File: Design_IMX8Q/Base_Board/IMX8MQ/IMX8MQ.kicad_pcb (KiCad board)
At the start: 8 copper layers, 50 x 80 mm, 95 parts, among them Q1 AO3401A, U1 MIMX8MQ6CVAHZAB, U2 IS43LQ32256A-062BLI, U4 MP8759GD-Z, U5 MP2263GD-Z, U6 SDINBDG4-8G, U7 MT25QUxxxxxx1xW7, X1 ABLNO, Y1 25MHz, Y2 27MHz

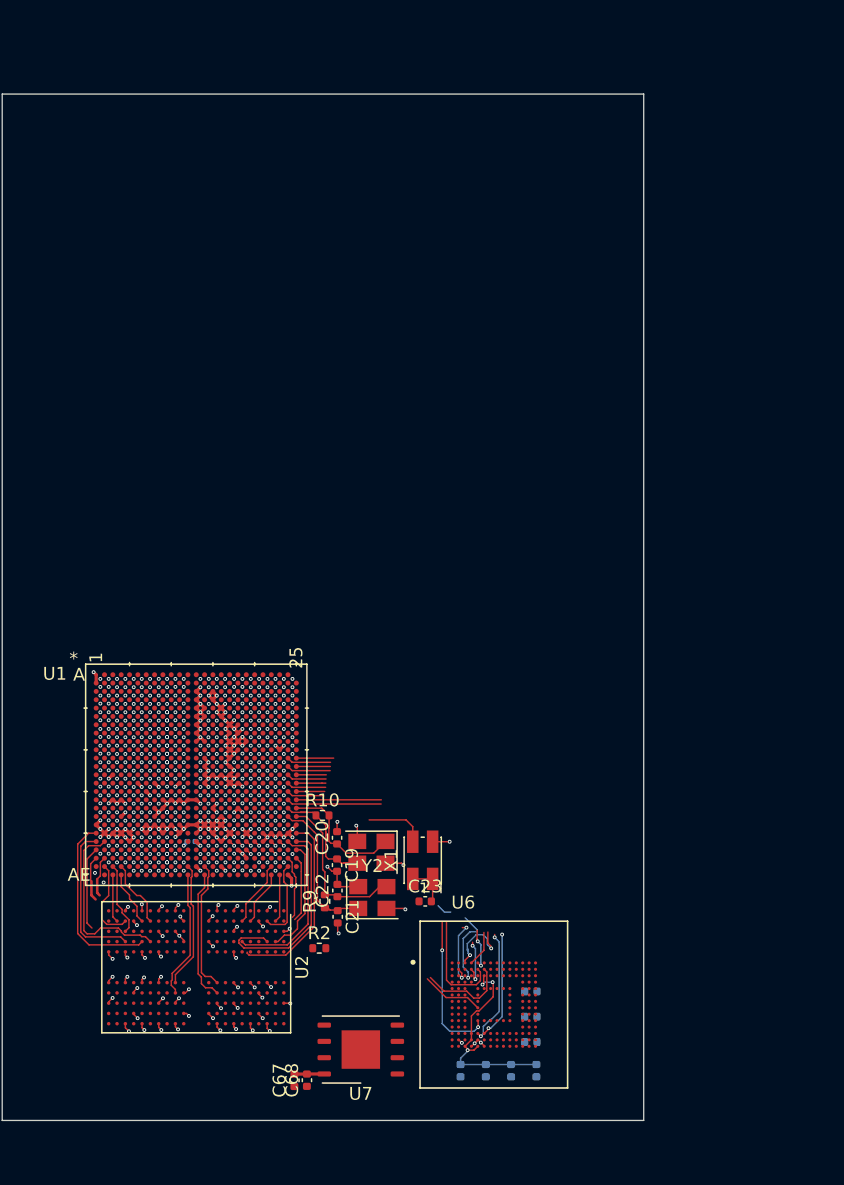
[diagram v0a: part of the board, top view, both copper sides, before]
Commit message: Adding color on LPDDR4 memory net
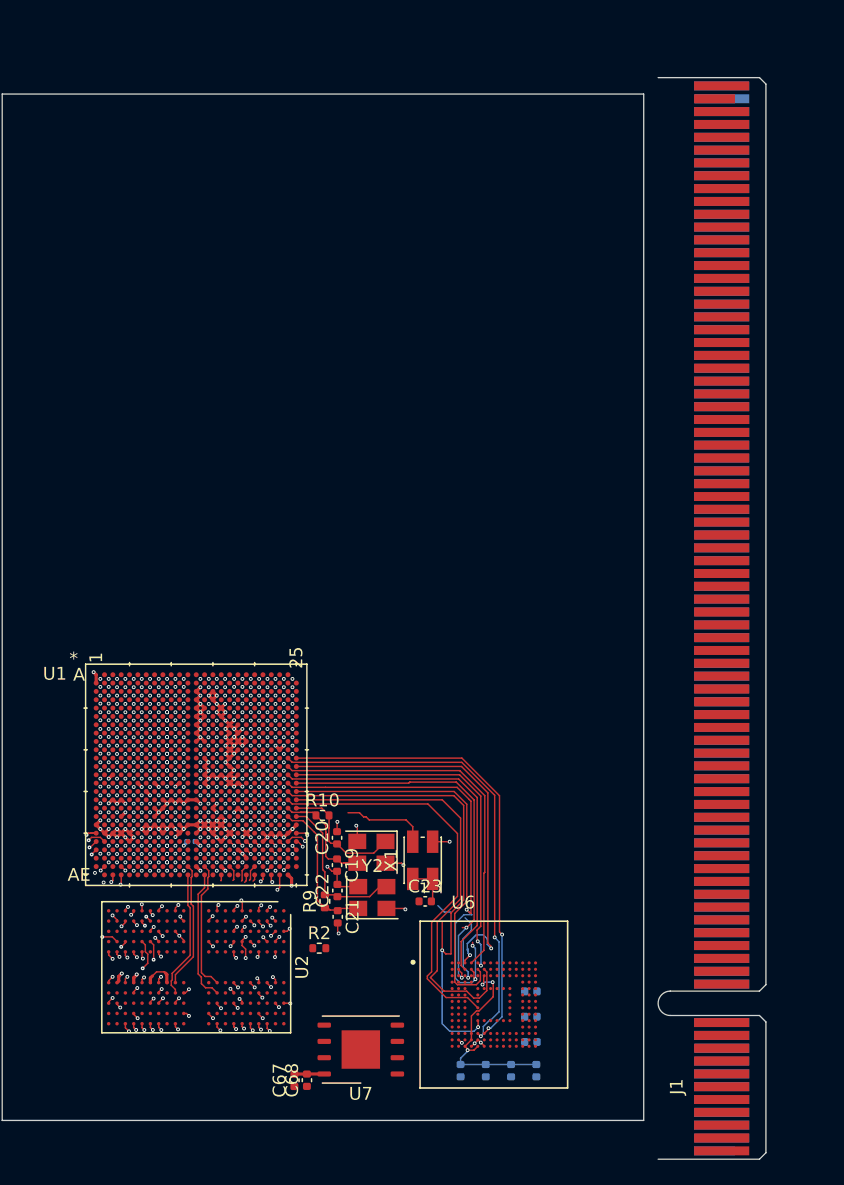
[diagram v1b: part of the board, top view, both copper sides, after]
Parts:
- added J1: Bus_PCI_Express_x16, Connector_PCBEdge:BUS_PCIexpress_x16, F.Cu at (114.0, 126.0)
- C24: value 0.1uF -> 4.7F
- C27: value 4.7F -> 0.1uF
- Y1: value 25MHz -> 27MHz
- Y2: value 27MHz -> 25MHz
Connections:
- U1 pad AB20: unconnected-(U1B-DRAM_DM1-PadAB20) -> DMI1_A
- U1 pad AB21: unconnected-(U1B-DRAM_DQS1_P-PadAB21) -> DQS1_A+
- U1 pad AB5: unconnected-(U1B-DRAM_DQS3_P-PadAB5) -> DQS1_B+
- U1 pad AB6: unconnected-(U1B-DRAM_DM3-PadAB6) -> DMI1_B
- U1 pad AC21: unconnected-(U1B-DRAM_DQS1_N-PadAC21) -> DQS1_A-
- U1 pad AC5: unconnected-(U1B-DRAM_DQS3_N-PadAC5) -> DQS1_B-
- U1 pad AC7: unconnected-(U1B-DRAM_AC28-PadAC7) -> CA2_B
- U1 pad AD17: unconnected-(U1B-DRAM_AC08-PadAD17) -> CA0_A
- U1 pad AD19: unconnected-(U1B-DRAM_AC12-PadAD19) -> CA4_A
- U1 pad AD20: unconnected-(U1B-DRAM_AC10-PadAD20) -> CA2_A
- U1 pad AD6: unconnected-(U1B-DRAM_AC31-PadAD6) -> CA5_B
- U1 pad AE16: unconnected-(U1B-DRAM_AC09-PadAE16) -> CA1_A
- U1 pad AE19: unconnected-(U1B-DRAM_AC13-PadAE19) -> CA5_A
- U1 pad AE20: unconnected-(U1B-DRAM_AC11-PadAE20) -> CA3_A
- U1 pad AE6: unconnected-(U1B-DRAM_AC30-PadAE6) -> CA4_B
- U1 pad AE7: unconnected-(U1B-DRAM_AC29-PadAE7) -> CA3_B
- U1 pad AE8: unconnected-(U1B-DRAM_AC32-PadAE8) -> CA0_B
- U1 pad AE9: unconnected-(U1B-DRAM_AC33-PadAE9) -> CA1_B
- U1 pad K10: unconnected-(U1H-VDD_GPU-PadK10) -> VDD_GPU
- U1 pad K12: unconnected-(U1H-VDD_SOC-PadK12) -> VDD_SOC
- U1 pad K13: unconnected-(U1K-VSSA_FPLL_ARM-PadK13) -> GND
- U1 pad K15: unconnected-(U1H-VDD_ARM-PadK15) -> VDD_ARM
- U1 pad K16: unconnected-(U1H-VDD_ARM-PadK16) -> VDD_ARM
- U1 pad L10: unconnected-(U1H-VDD_GPU-PadL10) -> VDD_GPU
- U1 pad L12: unconnected-(U1H-VDD_SOC-PadL12) -> VDD_SOC
- U1 pad L13: unconnected-(U1H-VDD_SOC-PadL13) -> VDD_SOC
- U1 pad L15: unconnected-(U1H-VDD_ARM-PadL15) -> VDD_ARM
- U1 pad L16: unconnected-(U1H-VDD_ARM-PadL16) -> VDD_ARM
- U1 pad M10: unconnected-(U1H-VDD_GPU-PadM10) -> VDD_GPU
- U1 pad M12: unconnected-(U1H-VDD_SOC-PadM12) -> VDD_SOC
- U1 pad M13: unconnected-(U1H-VDD_SOC-PadM13) -> VDD_SOC
- U1 pad M15: unconnected-(U1H-VDD_ARM-PadM15) -> VDD_ARM
- U1 pad M16: unconnected-(U1H-VDD_ARM-PadM16) -> VDD_ARM
- U1 pad N10: unconnected-(U1H-VDD_VPU-PadN10) -> VDD_VPU
- U1 pad N12: unconnected-(U1K-VSSA_SPLL_VIDEO2-PadN12) -> GND
- U1 pad N13: unconnected-(U1H-VDD_SOC-PadN13) -> VDD_SOC
- U1 pad P10: unconnected-(U1H-VDD_VPU-PadP10) -> VDD_VPU
- U1 pad P12: unconnected-(U1H-VDD_SOC-PadP12) -> VDD_SOC
- U1 pad P13: unconnected-(U1H-VDD_SOC-PadP13) -> VDD_SOC
- U1 pad P15: unconnected-(U1H-VDD_SOC-PadP15) -> VDD_SOC
- U1 pad P16: unconnected-(U1H-VDD_SOC-PadP16) -> VDD_SOC
- U1 pad R10: unconnected-(U1H-VDD_SOC-PadR10) -> VDD_SOC
- U1 pad R11: unconnected-(U1H-VDD_SOC-PadR11) -> VDD_SOC
- U1 pad R12: unconnected-(U1H-VDD_SOC-PadR12) -> VDD_SOC
- U1 pad R13: unconnected-(U1H-VDD_SOC-PadR13) -> VDD_SOC
- U1 pad R14: unconnected-(U1H-VDD_SOC-PadR14) -> VDD_SOC
- U1 pad R15: unconnected-(U1H-VDD_SOC-PadR15) -> VDD_SOC
- U1 pad R16: unconnected-(U1H-VDD_SOC-PadR16) -> VDD_SOC
- U1 pad T14: unconnected-(U1K-VSSA_SPLL_DRAM-PadT14) -> GND
- U1 pad T17: unconnected-(U1H-VDD_SOC-PadT17) -> VDD_SOC
- U1 pad U16: unconnected-(U1K-VSSA_FPLL-PadU16) -> GND
- U1 pad V17: unconnected-(U1K-VSSA_SPLL-PadV17) -> GND
- U1 pad V23: unconnected-(U1K-VSSA_XTAL_25M-PadV23) -> GND
- U1 pad W22: unconnected-(U1K-VSSA_XTAL_27M-PadW22) -> GND
- U2 pad AA11: unconnected-(U2B-DQ8_B-PadAA11) -> DRAM_DATA8_B
- U2 pad AA9: unconnected-(U2B-DQ15_B-PadAA9) -> DRAM_DATA15_B
- U2 pad B11: unconnected-(U2A-DQ8_A-PadB11) -> DRAM_DATA8_A
- U2 pad B9: unconnected-(U2A-DQ15_A-PadB9) -> DRAM_DATA15_A
- U2 pad C10: unconnected-(U2A-DMI1_A-PadC10) -> DMI1_A
- U2 pad C11: unconnected-(U2A-DQ9_A-PadC11) -> DRAM_DATA9_A
- U2 pad C9: unconnected-(U2A-DQ14_A-PadC9) -> DRAM_DATA14_A
- U2 pad D10: unconnected-(U2A-DQS1_T_A-PadD10) -> DQS1_A+
- U2 pad E10: unconnected-(U2A-DQS1_C_A-PadE10) -> DQS1_A-
- U2 pad E11: unconnected-(U2A-DQ10_A-PadE11) -> DRAM_DATA10_A
- U2 pad E9: unconnected-(U2A-DQ13_A-PadE9) -> DRAM_DATA13_A
- U2 pad F11: unconnected-(U2A-DQ11_A-PadF11) -> DRAM_DATA11_A
- U2 pad F9: unconnected-(U2A-DQ12_A-PadF9) -> DRAM_DATA12_A
- U2 pad H10: unconnected-(U2A-CA3_A-PadH10) -> CA3_A
- U2 pad H11: unconnected-(U2A-CA4_A-PadH11) -> CA4_A
- U2 pad H2: unconnected-(U2A-CA0_A-PadH2) -> CA0_A
- U2 pad H9: unconnected-(U2A-CA2_A-PadH9) -> CA2_A
- U2 pad J11: unconnected-(U2A-CA5_A-PadJ11) -> CA5_A
- U2 pad J2: unconnected-(U2A-CA1_A-PadJ2) -> CA1_A
- U2 pad P11: unconnected-(U2B-CA5_B-PadP11) -> CA5_B
- U2 pad P2: unconnected-(U2B-CA1_B-PadP2) -> CA1_B
- U2 pad R10: unconnected-(U2B-CA3_B-PadR10) -> CA3_B
- U2 pad R11: unconnected-(U2B-CA4_B-PadR11) -> CA4_B
- U2 pad R2: unconnected-(U2B-CA0_B-PadR2) -> CA0_B
- U2 pad R9: unconnected-(U2B-CA2_B-PadR9) -> CA2_B
- U2 pad U11: unconnected-(U2B-DQ11_B-PadU11) -> DRAM_DATA11_B
- U2 pad U9: unconnected-(U2B-DQ12_B-PadU9) -> DRAM_DATA12_B
- U2 pad V10: unconnected-(U2B-DQS1_C_B-PadV10) -> DQS1_B-
- U2 pad V11: unconnected-(U2B-DQ10_B-PadV11) -> DRAM_DATA10_B
- U2 pad V9: unconnected-(U2B-DQ13_B-PadV9) -> DRAM_DATA13_B
- U2 pad W10: unconnected-(U2B-DQS1_T_B-PadW10) -> DQS1_B+
- U2 pad Y10: unconnected-(U2B-DMI1_B-PadY10) -> DMI1_B
- U2 pad Y11: unconnected-(U2B-DQ9_B-PadY11) -> DRAM_DATA9_B
- U2 pad Y9: unconnected-(U2B-DQ14_B-PadY9) -> DRAM_DATA14_B
- Y1 pad 1: Net-(U1F-XTALI_25M) -> Net-(U1F-XTALO_27M)
- Y1 pad 3: Net-(U1F-XTALO_25M) -> Net-(U1F-XTALI_27M)
- Y2 pad 1: Net-(U1F-XTALO_27M) -> Net-(U1F-XTALI_25M)
- Y2 pad 3: Net-(U1F-XTALI_27M) -> Net-(U1F-XTALO_25M)
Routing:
- net SD1_DATA5: track 6.90 -> 36.1 mm, vias 2 -> 3
- net SD1_DATA4: track 10.3 -> 36.0 mm
- net SD1_CLK: track 11.3 -> 36.3 mm
- net SD1_CMD: track 12.5 -> 37.2 mm
- net SD1_nRST: track 14.5 -> 38.5 mm
- net SD1_DATA0: track 8.78 -> 32.8 mm
- net SD1_DATA1: track 6.20 -> 29.8 mm
- net VDD_1v8: track 0.00 -> 23.3 mm, vias 0 -> 27
- net SD1_DATA2: track 5.56 -> 28.9 mm
- net SD1_DATA3: track 7.61 -> 30.0 mm
- net SD1_DATA6: track 10.7 -> 31.1 mm
- net SD1_DATA7: track 13.7 -> 33.8 mm
- net SD1_STROBE: track 12.3 -> 31.5 mm
- net DMI0_B: track 5.69 -> 0.00 mm
- net DRAM_DATA6_A: track 16.7 -> 11.4 mm, vias 0 -> 2
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- added copper zone on In2.Cu, net VDD_1v8

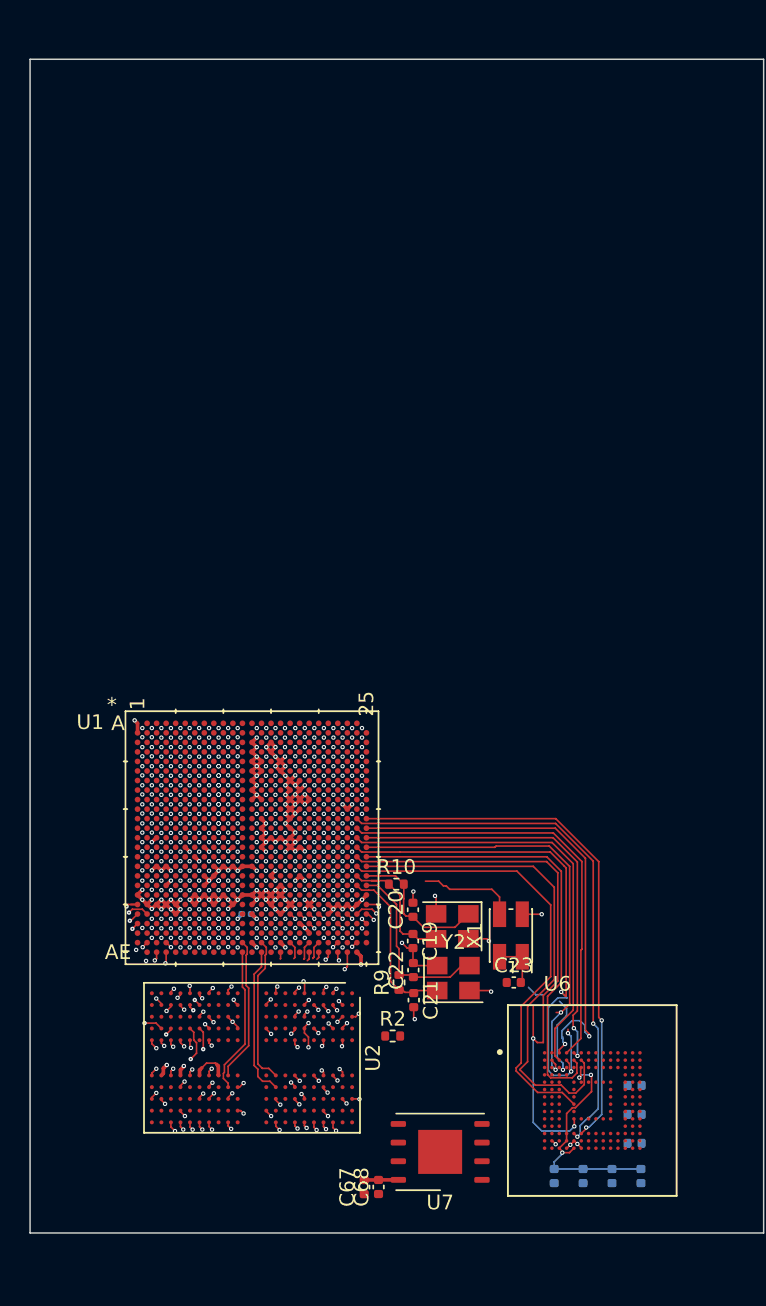
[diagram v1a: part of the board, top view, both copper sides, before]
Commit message: Add library to WIFI/BLE
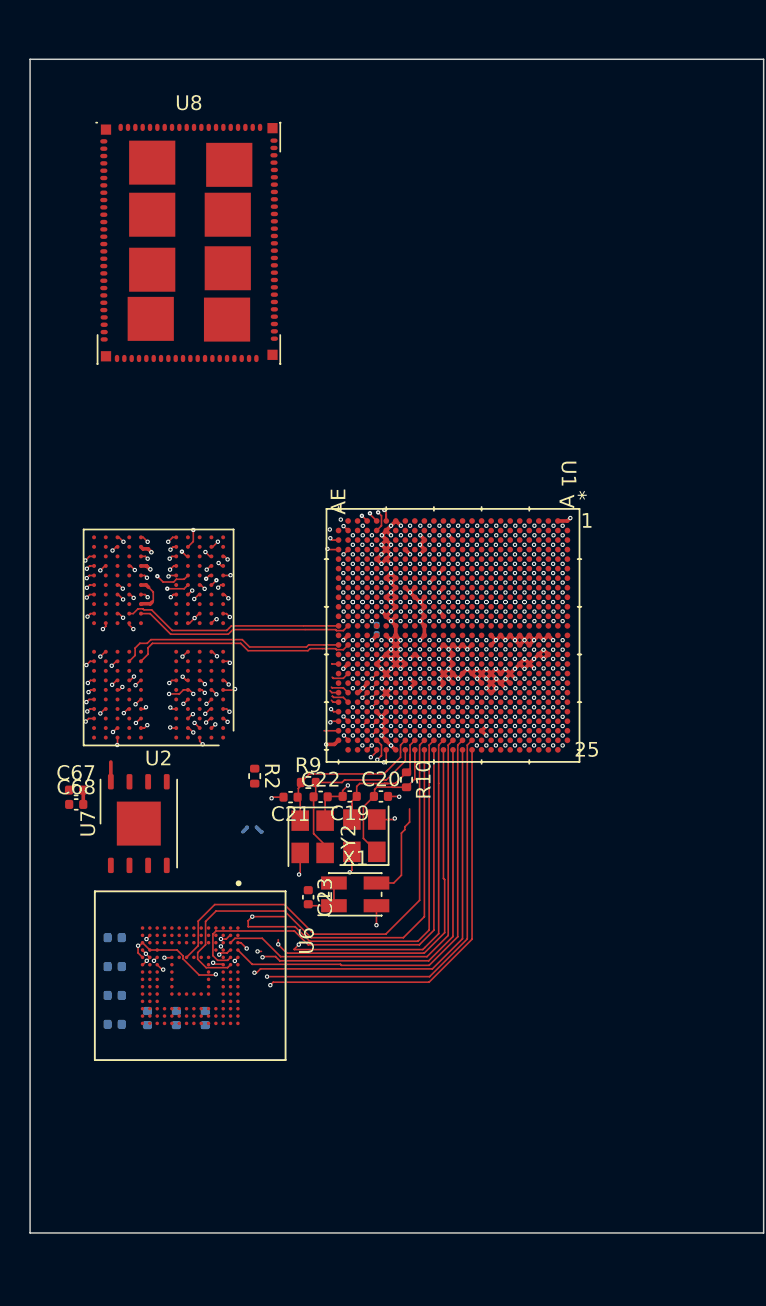
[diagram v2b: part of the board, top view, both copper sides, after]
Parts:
- added U8: ~, _W_SBC:WG3221-00_DTS_R01, F.Cu at (68.7, 56.2)
- moved C24 37.3 mm to (63.7, 109.4), turned to 0 degrees
- moved C25 36.1 mm to (63.7, 107.4), turned to 0 degrees
- moved C26 35.0 mm to (63.7, 105.5), turned to 0 degrees
- moved C28 34.3 mm to (65.9, 109.0), turned to -90 degrees
- moved C27 34.1 mm to (63.7, 103.5), turned to 0 degrees
- moved C67 33.4 mm to (61.0, 93.4), turned to 0 degrees
- moved C68 33.2 mm to (61.0, 94.4), turned to 0 degrees
- moved C29 31.9 mm to (67.9, 109.0), turned to -90 degrees
- moved U7 30.4 mm to (65.3, 95.7), turned to 90 degrees
- moved C30 29.6 mm to (69.8, 109.0), turned to -90 degrees
- moved U2 29.3 mm to (66.7, 83.0), turned to 180 degrees
- moved U6 28.7 mm to (68.8, 106.1), turned to -90 degrees
- moved R1 21.3 mm to (81.5, 82.5), turned to 90 degrees
- moved R2 20.1 mm to (73.2, 92.5), turned to -90 degrees
- moved U1 19.4 mm to (86.7, 82.9), turned to -90 degrees
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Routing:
- net DRAM_DATA4_B: track 17.6 -> 2.98 mm
- net DRAM_DATA5_B: track 18.1 -> 3.70 mm
- net DRAM_DATA4_A: track 16.1 -> 3.46 mm
- net DRAM_DATA5_A: track 14.0 -> 1.35 mm
- net SD1_DATA5: track 36.1 -> 25.2 mm
- net DRAM_DATA6_A: track 11.4 -> 1.20 mm
- net DRAM_DATA6_B: track 11.3 -> 1.13 mm
- net VDD_1v8: track 23.3 -> 13.6 mm
- net SD1_nRST: track 38.5 -> 29.6 mm
- net SD1_CMD: track 37.2 -> 28.7 mm
- net DRAM_DATA7_A: track 9.45 -> 1.05 mm
- net NVCC_SD1_1V8: track 16.2 -> 8.04 mm
- net SD1_CLK: track 36.3 -> 28.5 mm
- net DRAM_DATA7_B: track 8.70 -> 1.83 mm
- net SD1_DATA4: track 36.0 -> 29.5 mm
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- removed copper zone on In2.Cu, net VDD_1v8
